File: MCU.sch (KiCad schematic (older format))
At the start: 60 parts, among them J12 Conn_02x05_Odd_Even, J16 DM3AT-SF-PEJM5, J17 Conn_02x05_Odd_Even, Q28 LBSS84LT1G, SW3 SW_Push, SW4 SW_Push, U10 ESP32-WROOM-32U, U16 CH340G, U6 STM32F730R8T6, U7 LY68L6400SLIT, U9 FS35ND01G-S1Y2QWFI000, Y1 Q13FC1350000400, Y2 24MHz, Y3 12MHz

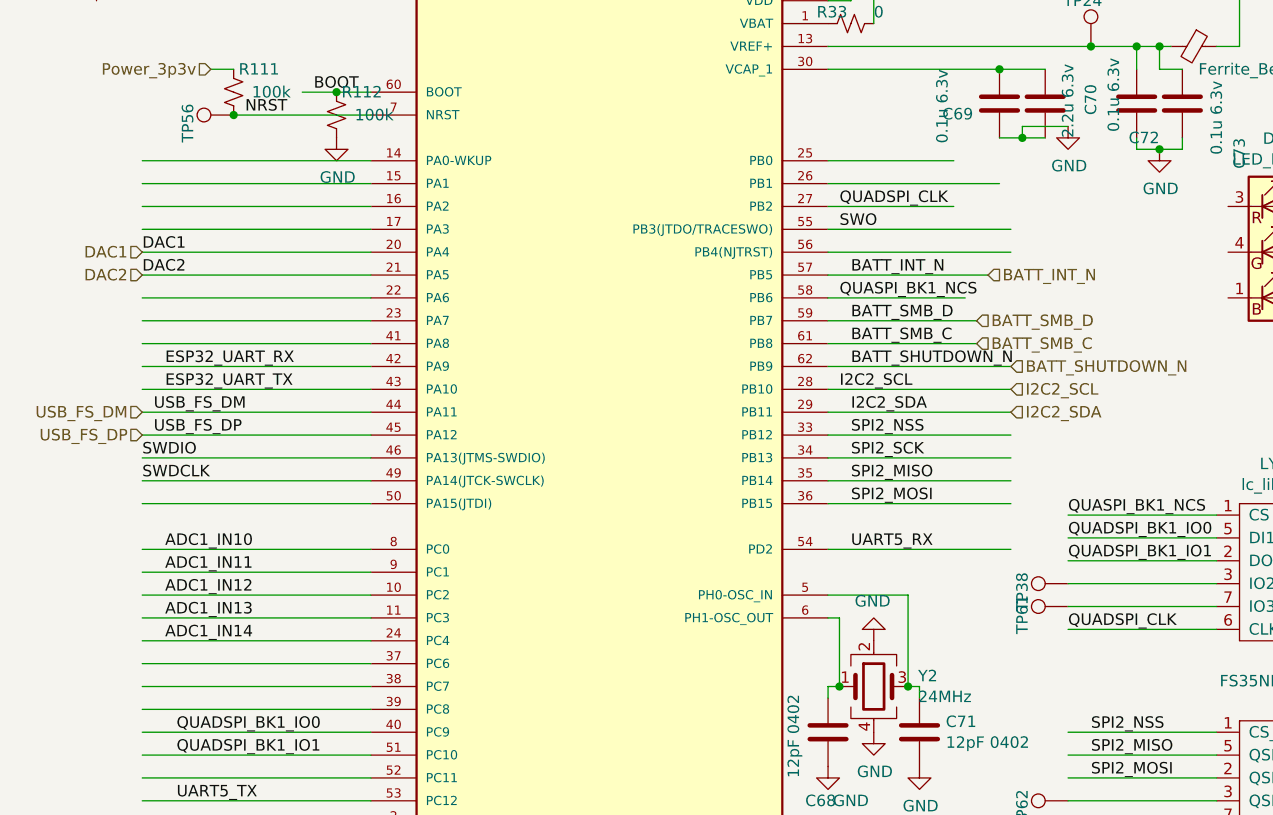
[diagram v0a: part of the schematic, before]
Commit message: Modified connections, added current limit
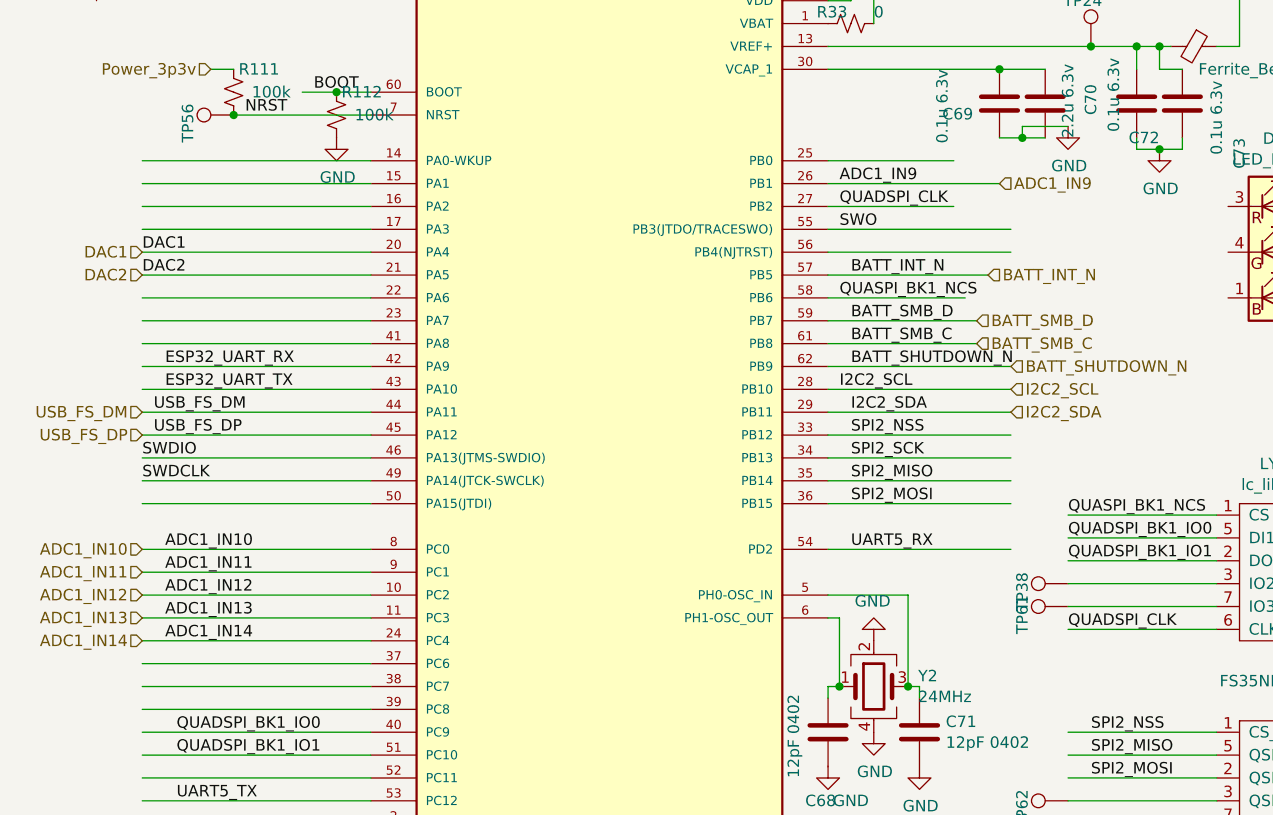
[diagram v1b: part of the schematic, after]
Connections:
- net labels added: ADC1_IN9
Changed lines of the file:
@@
 	1    0    0    -1
 $EndComp
+Text HLabel 900  3200 0    50   Input ~ 0
+ADC1_IN10
+Text HLabel 900  3300 0    50   Input ~ 0
+ADC1_IN11
+Text HLabel 900  3400 0    50   Input ~ 0
+ADC1_IN12
+Text HLabel 900  3500 0    50   Input ~ 0
+ADC1_IN13
+Text HLabel 900  3600 0    50   Input ~ 0
+ADC1_IN14
+Text Label 3950 1600 0    50   ~ 0
+ADC1_IN9
+Text HLabel 4650 1600 2    50   Input ~ 0
+ADC1_IN9
 $EndSCHEMATC
